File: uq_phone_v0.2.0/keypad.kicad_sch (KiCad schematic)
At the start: 60 parts, among them SW1 SKTAAAE010, SW10 SKTAAAE010, SW11 SKTAAAE010, SW12 SKTAAAE010, SW13 SKTAAAE010, SW14 SKTAAAE010, SW15 SKTAAAE010, SW16 SKTAAAE010, SW17 SKTAAAE010, SW18 SKTAAAE010, SW19 SKTAAAE010, SW2 SKTAAAE010, SW20 SKTAAAE010, SW21 SKTAAAE010, SW22 SKTAAAE010, SW23 SKTAAAE010, SW24 SKTAAAE010, SW25 SKTAAAE010, SW27 SKTAAAE010, SW29 SKTAAAE010, SW3 SKTAAAE010, SW31 SKTAAAE010, SW33 SKTAAAE010, SW34 SKTAAAE010, SW35 SKTAAAE010, SW36 SKTAAAE010, SW37 SKTAAAE010, SW38 SKTAAAE010, SW39 SKTAAAE010, SW4 SKTAAAE010, SW40 SKTAAAE010, SW41 SKTAAAE010, SW42 SKTAAAE010, SW43 SKSCLCE010, SW44 SKSCLCE010, SW45 SKSCLCE010, SW5 SKTAAAE010, SW6 SKTAAAE010, SW7 SKTAAAE010, SW8 SKTAAAE010, SW9 SKTAAAE010

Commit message: Clean repo
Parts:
- removed R23: 0R, Resistor_SMD:R_0603_1608Metric, symbol Resistors:Resistor_0R
- LED1, LED17: now fitted; now in the parts list
- LED10: renamed from LED9; now fitted; now in the parts list
- LED11: renamed from LED15; now fitted; now in the parts list
- LED12: renamed from LED5; now fitted; now in the parts list
- LED13: renamed from LED10; now fitted; now in the parts list
- LED14: renamed from LED16; now fitted; now in the parts list
- LED15: renamed from LED6; now fitted; now in the parts list
- LED16: renamed from LED11; now fitted; now in the parts list
- LED2: renamed from LED12; now fitted; now in the parts list
- LED3: renamed from LED2; now fitted; now in the parts list
- LED4: renamed from LED7; now fitted; now in the parts list
- LED5: renamed from LED13; now fitted; now in the parts list
- LED6: renamed from LED3; now fitted; now in the parts list
- LED7: renamed from LED8; now fitted; now in the parts list
- LED8: renamed from LED14; now fitted; now in the parts list
- LED9: renamed from LED4; now fitted; now in the parts list
- R42: renamed from R48; now fitted; now in the parts list
- SW1: renamed from SW19; now fitted; now in the parts list
- SW10: renamed from SW38; now fitted; now in the parts list
- SW11: renamed from SW34; now fitted; now in the parts list
- SW12: renamed from SW13; now fitted; now in the parts list
- SW13: renamed from SW15; now fitted; now in the parts list
- SW14: renamed from SW17; now fitted; now in the parts list
- SW15: renamed from SW41; now fitted; now in the parts list
- SW16: renamed from SW45; now fitted; now in the parts list
- SW17: renamed from SW31; now fitted; now in the parts list
- SW18: renamed from SW14; now fitted; now in the parts list
- SW19: renamed from SW16; now fitted; now in the parts list
- SW2: renamed from SW21; now fitted; now in the parts list
- SW20: renamed from SW18; now fitted; now in the parts list
- SW21: renamed from SW42; now fitted; now in the parts list
- SW22: renamed from SW44; now fitted; now in the parts list
- SW23: renamed from SW27; now fitted; now in the parts list
- SW24: renamed from SW7; now fitted; now in the parts list
- SW25: renamed from SW9; now fitted; now in the parts list
- SW26: renamed from SW11; now fitted; now in the parts list
- SW27: renamed from SW35; now fitted; now in the parts list
- SW28: renamed from SW8; now fitted; now in the parts list
- SW29: renamed from SW10; now fitted; now in the parts list
- SW3: renamed from SW23; now fitted; now in the parts list
- SW30: renamed from SW12; now fitted; now in the parts list
- SW31: renamed from SW36; now fitted; now in the parts list
- SW32: renamed from SW29; now fitted; now in the parts list
- SW33: renamed from SW1; now fitted; now in the parts list
- SW34: renamed from SW3; now fitted; now in the parts list
- SW35: renamed from SW5; now fitted; now in the parts list
- SW36: renamed from SW39; now fitted; now in the parts list
- SW37: renamed from SW25; now fitted; now in the parts list
- SW38: renamed from SW2; now fitted; now in the parts list
- SW39: renamed from SW4; now fitted; now in the parts list
- SW4: renamed from SW37; now fitted; now in the parts list
- SW40: renamed from SW6; now fitted; now in the parts list
- SW41: renamed from SW40; now fitted; now in the parts list
- SW5: renamed from SW33; now fitted; now in the parts list
- SW6: renamed from SW43; now fitted; now in the parts list
- SW7: renamed from SW20; now fitted; now in the parts list
- SW8: renamed from SW22; now fitted; now in the parts list
- SW9: renamed from SW24; now fitted; now in the parts list
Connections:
- net VLED is gone; now on net +3.3V: LED1.2 (VDD), LED10.2 (VDD), LED11.2 (VDD), LED12.2 (VDD), LED13.2 (VDD), LED14.2 (VDD), LED15.2 (VDD), LED16.2 (VDD), LED17.2 (VDD), LED2.2 (VDD), LED3.2 (VDD), LED4.2 (VDD), LED5.2 (VDD), LED6.2 (VDD), LED7.2 (VDD), LED8.2 (VDD), LED9.2 (VDD)

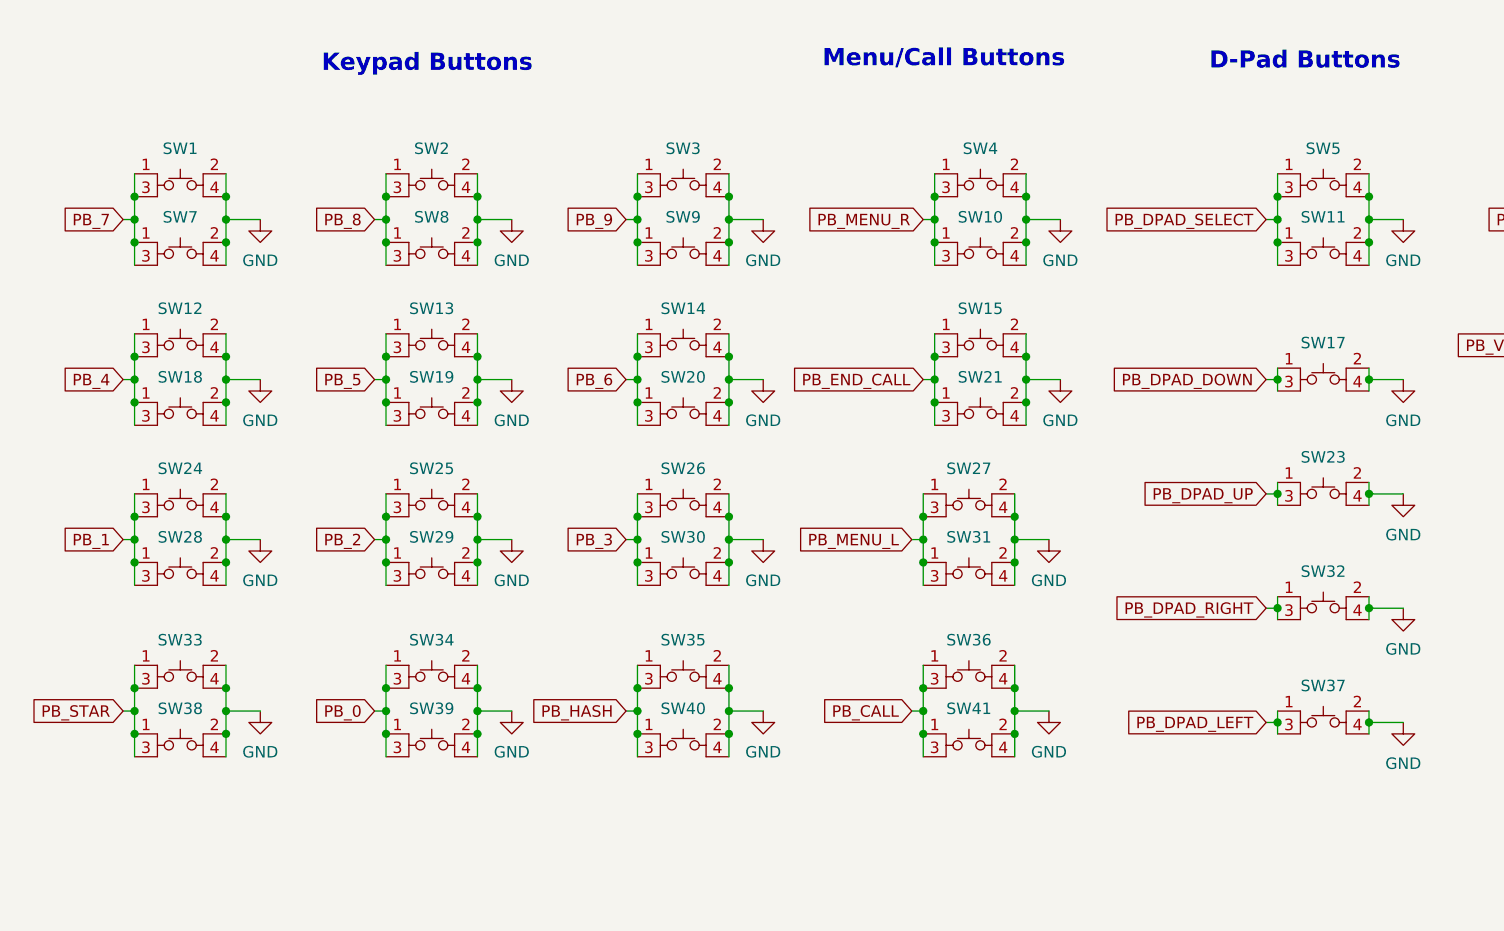
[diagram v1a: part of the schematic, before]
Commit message: Add more footprints, reduce sizes
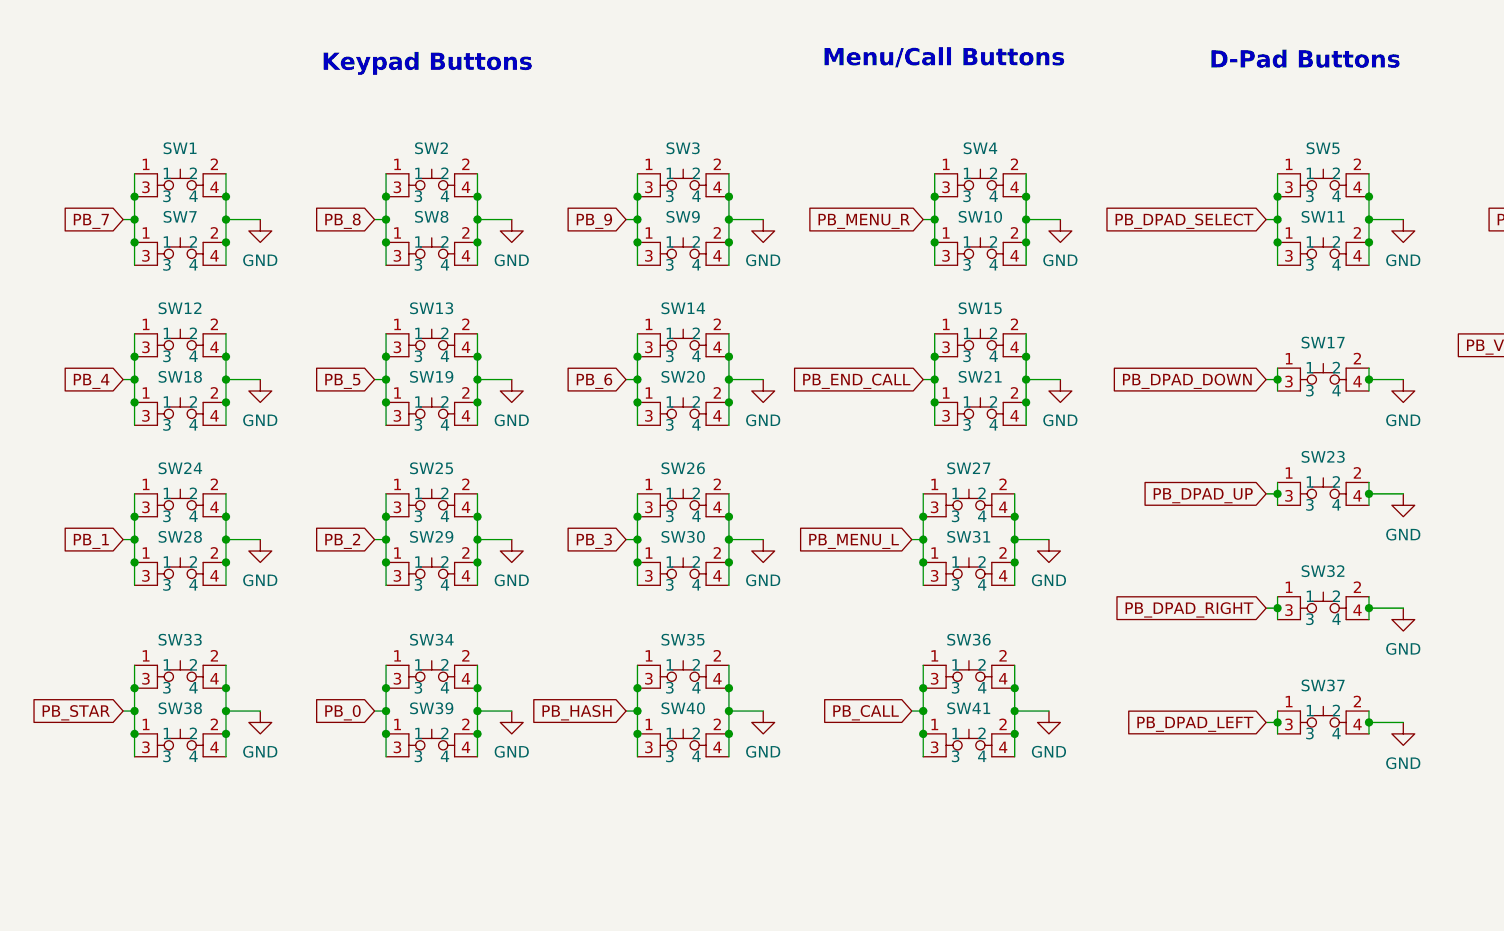
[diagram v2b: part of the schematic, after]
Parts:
- LED1, LED10, LED11, LED12, LED13, LED14, LED15, LED16, LED17, LED2, LED3, LED4, LED5, LED6, LED7, LED8, LED9: LCSC PN (none) -> C5349953
- SW1, SW10, SW11, SW12, SW13, SW14, SW15, SW17, SW18, SW19, SW2, SW20, SW21, SW23, SW24, SW25, SW26, SW27, SW28, SW29, SW3, SW30, SW31, SW32, SW33, SW34, SW35, SW36, SW37, SW38, SW39, SW4, SW40, SW41, SW5, SW7, SW8, SW9: LCSC PN (none) -> C358616
- SW16, SW22, SW6: LCSC PN (none) -> C139799
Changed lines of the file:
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@@
 			)
 		)
-		(property "LSCS PN" ""
+		(property "LCSC PN" "C5349953"
 			(at 358.14 199.39 0)
 			(effects
@@
 			)
 		)
-		(property "LSCS PN" ""
+		(property "LCSC PN" "C358616"
 			(at 128.27 92.71 0)
 			(effects
@@
 			)
 		)
-		(property "LSCS PN" ""
+		(property "LCSC PN" "C5349953"
 			(at 358.14 175.26 0)
 			(effects
@@
 			)
 		)
-		(property "LSCS PN" ""
+		(property "LCSC PN" "C358616"
 			(at 127 135.89 0)
 			(effects
@@
 			)
 		)
-		(property "LSCS PN" ""
+		(property "LCSC PN" "C358616"
 			(at 127 147.32 0)
 			(effects
@@
 			)
 		)
-		(property "LSCS PN" ""
+		(property "LCSC PN" "C139799"
 			(at 209.55 111.76 0)
 			(effects
@@
 			)
 		)
-		(property "LSCS PN" ""
+		(property "LCSC PN" "C358616"
 			(at 67.31 135.89 0)
 			(effects
@@
 			)
 		)
-		(property "LSCS PN" ""
+		(property "LCSC PN" "C358616"
 			(at 127 128.27 0)
 			(effects
@@
 			)
 		)
-		(property "LSCS PN" ""
+		(property "LCSC PN" "C358616"
 			(at 67.31 154.94 0)
 			(effects
@@
 			)
 		)
-		(property "LSCS PN" ""
+		(property "LCSC PN" "C358616"
 			(at 67.31 92.71 0)
 			(effects
@@
 			)
 		)
-		(property "LSCS PN" ""
+		(property "LCSC PN" "C358616"
 			(at 95.25 147.32 0)
 			(effects
@@
 			)
 		)
-		(property "LSCS PN" ""
+		(property "LCSC PN" "C358616"
 			(at 128.27 118.11 0)
 			(effects
@@
 			)
 		)
-		(property "LSCS PN" ""
+		(property "LCSC PN" "C358616"
 			(at 39.37 154.94 0)
 			(effects
@@
 			)
 		)
-		(property "LSCS PN" ""
+		(property "LCSC PN" "C358616"
 			(at 67.31 128.27 0)
 			(effects
@@
 			)
 		)
-		(property "LSCS PN" ""
+		(property "LCSC PN" "C358616"
 			(at 95.25 92.71 0)
 			(effects
@@
 			)
 		)
-		(property "LSCS PN" ""
+		(property "LCSC PN" "C358616"
 			(at 67.31 110.49 0)
 			(effects
@@
 			)
 		)
-		(property "LSCS PN" ""
+		(property "LCSC PN" "C358616"
 			(at 39.37 128.27 0)
 			(effects
@@
 			)
 		)
-		(property "LSCS PN" ""
+		(property "LCSC PN" "C358616"
 			(at 67.31 100.33 0)
 			(effects
@@
 			)
 		)
-		(property "LSCS PN" ""
+		(property "LCSC PN" "C358616"
 			(at 166.37 139.7 0)
 			(effects
@@
 			)
 		)
-		(property "LSCS PN" ""
+		(property "LCSC PN" "C5349953"
 			(at 314.96 78.74 0)
 			(effects
@@
 			)
 		)
-		(property "LSCS PN" ""
+		(property "LCSC PN" "C5349953"
 			(at 336.55 199.39 0)
 			(effects
@@
 			)
 		)
-		(property "LSCS PN" ""
+		(property "LCSC PN" "C358616"
 			(at 166.37 100.33 0)
 			(effects
@@
 			)
 		)
-		(property "LSCS PN" ""
+		(property "LCSC PN" "C358616"
 			(at 166.37 92.71 0)
 			(effects
@@
 			)
 		)
-		(property "LSCS PN" ""
+		(property "LCSC PN" "C5349953"
 			(at 358.14 151.13 0)
 			(effects
@@
 			)
 		)
-		(property "LSCS PN" ""
+		(property "LCSC PN" "C358616"
 			(at 166.37 127 0)
 			(effects
@@
 			)
 		)
-		(property "LSCS PN" ""
+		(property "LCSC PN" "C358616"
 			(at 128.27 110.49 0)
 			(effects
@@
 			)
 		)
-		(property "LSCS PN" ""
+		(property "LCSC PN" "C5349953"
 			(at 358.14 127 0)
 			(effects
@@
 			)
 		)
-		(property "LSCS PN" ""
+		(property "LCSC PN" "C5349953"
 			(at 336.55 151.13 0)
 			(effects
@@
 			)
 		)
-		(property "LSCS PN" ""
+		(property "LCSC PN" "C5349953"
 			(at 336.55 175.26 0)
 			(effects
@@
 			)
 		)
-		(property "LSCS PN" ""
+		(property "LCSC PN" "C5349953"
 			(at 314.96 175.26 0)
 			(effects
@@
 			)
 		)
-		(property "LSCS PN" ""
+		(property "LCSC PN" "C358616"
 			(at 95.25 118.11 0)
 			(effects
@@
 			)
 		)
-		(property "LSCS PN" ""
+		(property "LCSC PN" "C358616"
 			(at 39.37 92.71 0)
 			(effects
@@
 			)
 		)
-		(property "LSCS PN" ""
+		(property "LCSC PN" "C5349953"
 			(at 336.55 102.87 0)
 			(effects
@@
 			)
 		)
-		(property "LSCS PN" ""
+		(property "LCSC PN" "C358616"
 			(at 39.37 135.89 0)
 			(effects
@@
 			)
 		)
-		(property "LSCS PN" ""
-			(at 306.07 196.85 90)
-			(effects
-				(font
-					(size 1.27 1.27)
-				)
-				(hide yes)
-			)
-		)
 		(pin "1"
 		)
@@
 			)
 		)
-		(property "LSCS PN" ""
+		(property "LCSC PN" "C5349953"
 			(at 314.96 102.87 0)
 			(effects
@@
 			)
 		)
-		(property "LSCS PN" ""
+		(property "LCSC PN" "C358616"
 			(at 39.37 147.32 0)
 			(effects
@@
 			)
 		)
-		(property "LSCS PN" ""
+		(property "LCSC PN" "C358616"
 			(at 166.37 114.3 0)
 			(effects
@@
 			)
 		)
-		(property "LSCS PN" ""
+		(property "LCSC PN" "C5349953"
 			(at 358.14 102.87 0)
 			(effects
@@
 			)
 		)
-		(property "LSCS PN" ""
+		(property "LCSC PN" "C5349953"
 			(at 314.96 151.13 0)
 			(effects
@@
 			)
 		)
-		(property "LSCS PN" ""
+		(property "LCSC PN" "C358616"
 			(at 128.27 100.33 0)
 			(effects
@@
 			)
 		)
-		(property "LSCS PN" ""
+		(property "LCSC PN" "C139799"
 			(at 209.55 97.79 0)
 			(effects
@@
 			)
 		)
-		(property "LSCS PN" ""
+		(property "LCSC PN" "C139799"
 			(at 209.55 124.46 0)
 			(effects
@@
 			)
 		)
-		(property "LSCS PN" ""
+		(property "LCSC PN" "C358616"
 			(at 95.25 100.33 0)
 			(effects
@@
 			)
 		)
-		(property "LSCS PN" ""
+		(property "LCSC PN" "C358616"
 			(at 95.25 128.27 0)
 			(effects
@@
 			)
 		)
-		(property "LSCS PN" ""
+		(property "LCSC PN" "C358616"
 			(at 166.37 152.4 0)
 			(effects
@@
 			)
 		)
-		(property "LSCS PN" ""
+		(property "LCSC PN" "C358616"
 			(at 95.25 110.49 0)
 			(effects
@@
 			)
 		)
-		(property "LSCS PN" ""
+		(property "LCSC PN" "C358616"
 			(at 39.37 118.11 0)
 			(effects
@@
 			)
 		)
-		(property "LSCS PN" ""
+		(property "LCSC PN" "C358616"
 			(at 95.25 154.94 0)
 			(effects
@@
 			)
 		)
-		(property "LSCS PN" ""
+		(property "LCSC PN" "C5349953"
 			(at 336.55 127 0)
 			(effects
@@
 			)
 		)
-		(property "LSCS PN" ""
+		(property "LCSC PN" "C358616"
 			(at 127 154.94 0)
 			(effects
@@
 			)
 		)
-		(property "LSCS PN" ""
+		(property "LCSC PN" "C358616"
 			(at 67.31 118.11 0)
 			(effects
@@
 			)
 		)
-		(property "LSCS PN" ""
+		(property "LCSC PN" "C5349953"
 			(at 314.96 199.39 0)
 			(effects
@@
 			)
 		)
-		(property "LSCS PN" ""
+		(property "LCSC PN" "C358616"
 			(at 67.31 147.32 0)
 			(effects
@@
 			)
 		)
-		(property "LSCS PN" ""
+		(property "LCSC PN" "C358616"
 			(at 39.37 100.33 0)
 			(effects
@@
 			)
 		)
-		(property "LSCS PN" ""
+		(property "LCSC PN" "C5349953"
 			(at 314.96 127 0)
 			(effects
@@
 			)
 		)
-		(property "LSCS PN" ""
+		(property "LCSC PN" "C5349953"
 			(at 358.14 78.74 0)
 			(effects
@@
 			)
 		)
-		(property "LSCS PN" ""
+		(property "LCSC PN" "C358616"
 			(at 95.25 135.89 0)
 			(effects
@@
 			)
 		)
-		(property "LSCS PN" ""
+		(property "LCSC PN" "C358616"
 			(at 39.37 110.49 0)
 			(effects

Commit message: Various Changes to footprints and components
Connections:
- net +3.3V renamed +3.3V_SW
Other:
- title: Power System -> UQ Phone
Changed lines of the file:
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@@
 	(paper "A3")
 	(title_block
-		(title "Power System")
+		(title "UQ Phone")
+		(rev "0.2.0")
 		(company "The University of Queensland")
 	)
@@
 	)
 	(symbol
-		(lib_id "power:+3.3V")
-		(at 337.82 52.07 0)
-		(mirror y)
-		(unit 1)
-		(exclude_from_sim no)
-		(in_bom yes)
-		(on_board yes)
-		(dnp no)
-		(fields_autoplaced yes)
-		(property "Reference" "#PWR0119"
-			(at 337.82 55.88 0)
-			(effects
-				(font
-					(size 1.27 1.27)
-				)
-				(hide yes)
-			)
-		)
-		(property "Value" "+3.3V"
-			(at 337.82 46.99 0)
-			(effects
-				(font
-					(size 1.27 1.27)
-				)
-			)
-		)
-		(property "Footprint" ""
-			(at 337.82 52.07 0)
-			(effects
-				(font
-					(size 1.27 1.27)
-				)
-				(hide yes)
-			)
-		)
-		(property "Datasheet" ""
-			(at 337.82 52.07 0)
-			(effects
-				(font
-					(size 1.27 1.27)
-				)
-				(hide yes)
-			)
-		)
-		(property "Description" "Power symbol creates a global label with name \"+3.3V\""
-			(at 337.82 52.07 0)
-			(effects
-				(font
-					(size 1.27 1.27)
-				)
-				(hide yes)
-			)
-		)
-		(pin "1"
-		)
-		(instances
-			(project "uq_phone"
-				(path "/14f57415-6807-40a5-bb38-3cb818a2cdae/f23e268a-469e-43b6-84c9-7924a6d2bdbb"
-					(reference "#PWR0119")
-					(unit 1)
-				)
-			)
-		)
-	)
-	(symbol
 		(lib_id "power:GND")
 		(at 180.34 115.57 0)
@@
 					(unit 1)
 				)
+			)
+		)
+	)
+	(symbol
+		(lib_id "power:+3.3V")
+		(at 337.82 52.07 0)
+		(unit 1)
+		(exclude_from_sim no)
+		(in_bom yes)
+		(on_board yes)
+		(dnp no)
+		(fields_autoplaced yes)
+		(property "Reference" "#PWR0119"
+			(at 337.82 55.88 0)
+			(effects
+				(font
+					(size 1.27 1.27)
+				)
+				(hide yes)
+			)
+		)
+		(property "Value" "+3.3V_SW"
+			(at 337.82 46.99 0)
+			(effects
+				(font
+					(size 1.27 1.27)
+				)
+			)
+		)
+		(property "Footprint" ""
+			(at 337.82 52.07 0)
+			(effects
+				(font
+					(size 1.27 1.27)
+				)
+				(hide yes)
+			)
+		)
+		(property "Datasheet" ""
+			(at 337.82 52.07 0)
+			(effects
+				(font
+					(size 1.27 1.27)
+				)
+				(hide yes)
+			)
+		)
+		(property "Description" "Power symbol creates a global label with name \"+3.3V\""
+			(at 337.82 52.07 0)
+			(effects
+				(font
+					(size 1.27 1.27)
+				)
+				(hide yes)
+			)
+		)
+		(pin "1"
+		)
+		(instances
+			(project "uq_phone"
+				(path "/14f57415-6807-40a5-bb38-3cb818a2cdae/f23e268a-469e-43b6-84c9-7924a6d2bdbb"
+					(reference "#PWR0119")
+					(unit 1)
+				)

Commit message: More routing and placements
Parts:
- added LED18, LED20, LED21, LED22, LED23, LED24, LED25, LED26, LED27, LED28, LED31: XL-1010RGBC, custom_footprints:XL-1010RGBC-WS2812B, symbol Misc:XL-1010RGBC-WS2812B
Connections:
- net +3.3V_SW: now also LED18.2 (VDD), LED20.2 (VDD), LED21.2 (VDD), LED22.2 (VDD), LED23.2 (VDD), LED24.2 (VDD), LED25.2 (VDD), LED26.2 (VDD), LED27.2 (VDD), LED28.2 (VDD), LED31.2 (VDD)
- net GND: now also LED18.3 (GND), LED20.3 (GND), LED21.3 (GND), LED22.3 (GND), LED23.3 (GND), LED24.3 (GND), LED25.3 (GND), LED26.3 (GND), LED27.3 (GND), LED28.3 (GND), LED31.3 (GND)
- net at LED13.1 (DO), LED14.4 (DI): now also LED31.4 (DI)
- new net: LED27.1 (DO), LED28.4 (DI)
- new net: LED26.1 (DO), LED27.4 (DI)
- new net: LED20.4 (DI), LED25.1 (DO)
- new net: LED24.1 (DO), LED25.4 (DI)
- new net: LED23.1 (DO), LED24.4 (DI)
- new net: LED23.4 (DI), LED28.1 (DO)
- new net: LED18.4 (DI), LED22.1 (DO)
- new net: LED26.4 (DI), LED31.1 (DO)
- new net: LED21.1 (DO), LED22.4 (DI)
- new net: LED20.1 (DO), LED21.4 (DI)
- no-connect marks 1 -> 2
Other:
- moved on the sheet: LED1, LED10, LED11, LED12, LED13, LED14, LED15, LED16, LED17, LED2, LED3, LED4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

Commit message: Another day of routing and adding components
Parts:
- added LED19: XL-1010RGBC, custom_footprints:XL-1010RGBC-Alt, symbol Misc:XL-1010RGBC-WS2812B
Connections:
- net +3.3V_SW: now also LED19.2 (VDD)
- net GND: now also LED19.3 (GND)
- net at LED18.1 (DO): now also LED19.4 (DI)
